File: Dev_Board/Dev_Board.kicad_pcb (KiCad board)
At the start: 2 copper layers, 48.9 x 67.6 mm, 28 parts, among them J1 Conn_01x04, J2 Conn_01x04

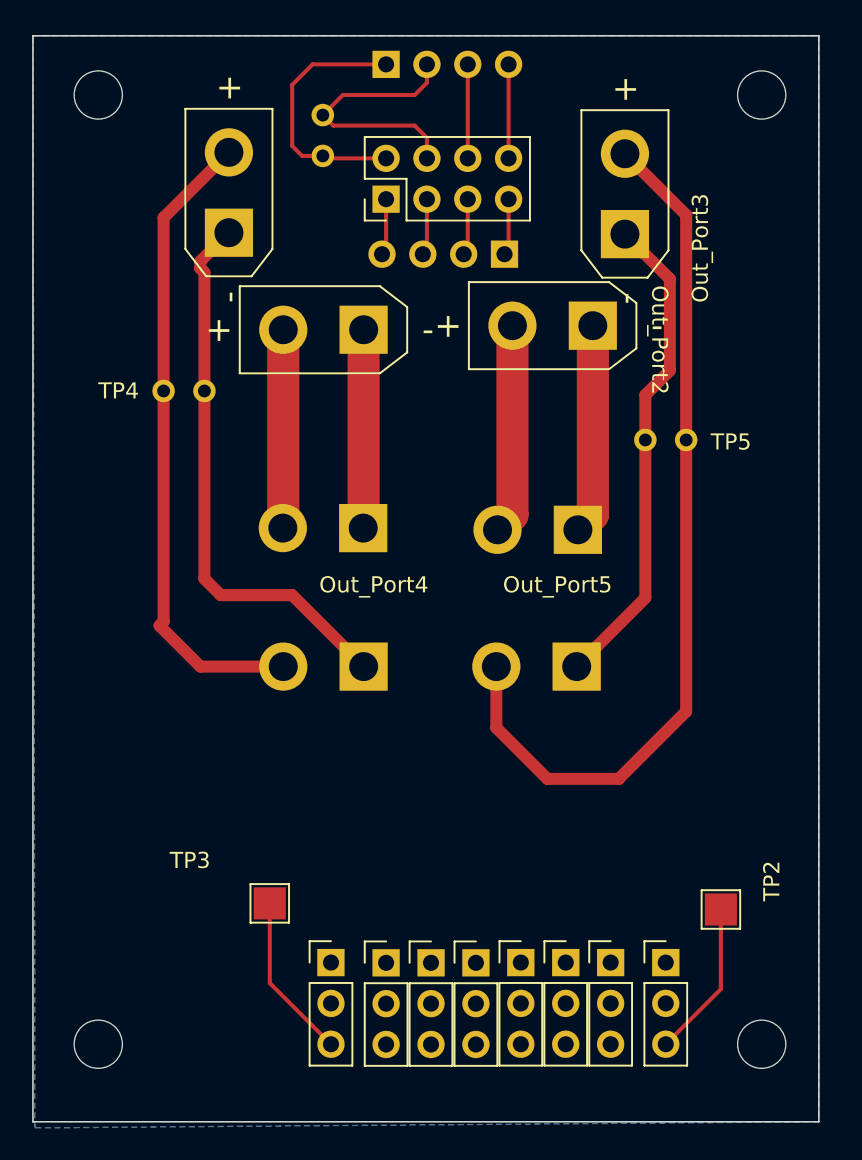
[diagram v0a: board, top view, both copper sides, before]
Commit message: added 24V plane and will resize pcb b/c dev board is 41mm
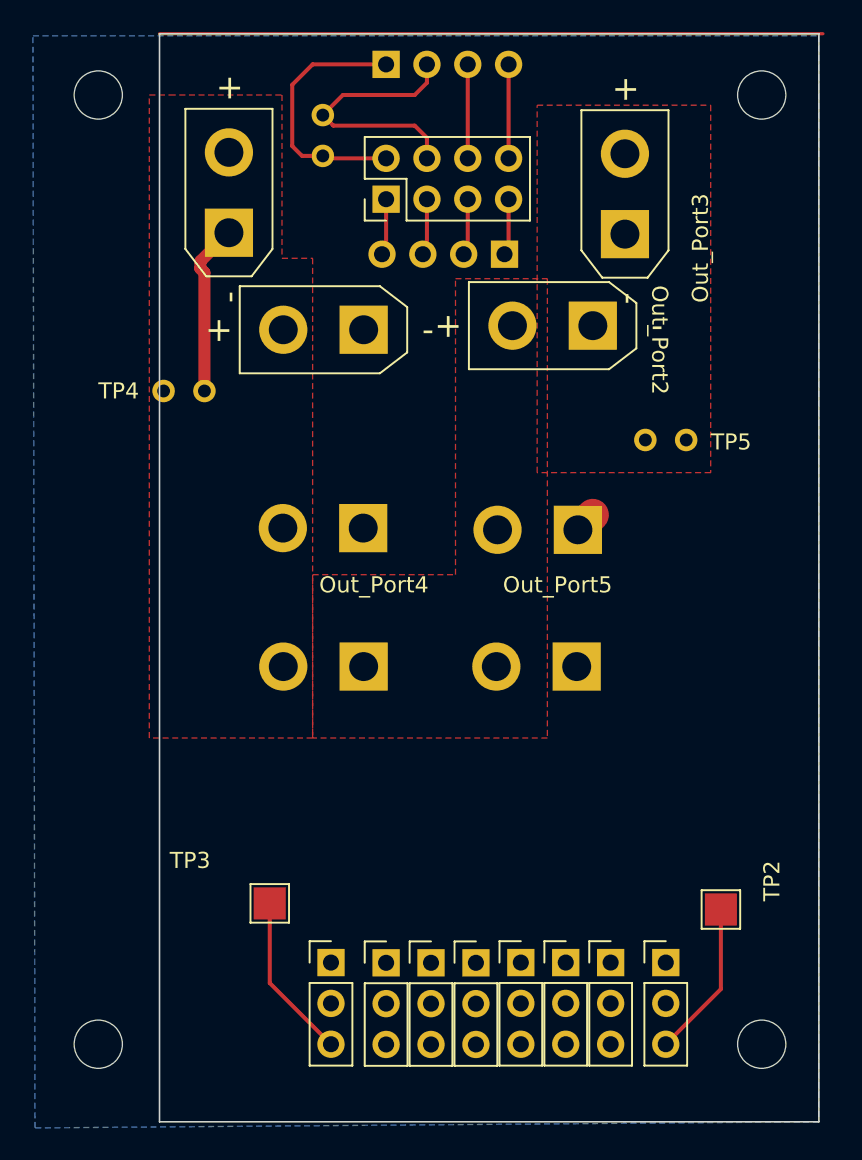
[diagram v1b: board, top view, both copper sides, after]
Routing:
- net +24V: track 120.4 -> 0.14 mm
- net GND: track 108.3 -> 29.9 mm
- added copper zone on F.Cu, net +24V
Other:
- board size 48.9 x 67.6 mm -> 41 x 67.7 mm
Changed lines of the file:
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@@
     )
   )
-  (gr_rect (start 178.181 29.972) (end 227.076 97.536)
+  (gr_line (start 186.055 29.845) (end 227.33 29.845)
+    (stroke (width 0.2) (type default)) (layer "F.Cu"))
+  (gr_rect (start 186.055 29.845) (end 227.076 97.536)
     (stroke (width 0.1) (type default)) (fill none) (layer "Edge.Cuts"))
   (segment (start 192.913 88.9) (end 196.723 92.71) (width 0.25) (layer "F.Cu") (net 1))
@@
   (segment (start 207.772 31.75) (end 207.772 37.597) (width 0.25) (layer "F.Cu") (net 27))
   (segment (start 205.232 31.75) (end 205.232 37.597) (width 0.25) (layer "F.Cu") (net 28))
-  (segment (start 218.821 41.121) (end 215.011 37.311) (width 0.75) (layer "F.Cu") (net 29))
-  (segment (start 188.595 69.215) (end 193.755 69.215) (width 0.75) (layer "F.Cu") (net 29))
-  (segment (start 218.821 55.118) (end 218.821 72.009) (width 0.75) (layer "F.Cu") (net 29))
-  (segment (start 207.01 73.025) (end 207.01 69.215) (width 0.75) (layer "F.Cu") (net 29))
-  (segment (start 208.013 48.006) (end 208.013 59.777) (width 2) (layer "F.Cu") (net 29))
   (segment (start 193.755 60.573) (end 193.728 60.6) (width 2) (layer "F.Cu") (net 29))
-  (segment (start 208.013 59.777) (end 207.084 60.706) (width 2) (layer "F.Cu") (net 29))
-  (segment (start 210.185 76.2) (end 207.01 73.025) (width 0.75) (layer "F.Cu") (net 29))
-  (segment (start 193.755 48.26) (end 193.755 60.573) (width 2) (layer "F.Cu") (net 29))
-  (segment (start 190.373 37.224) (end 186.309 41.288) (width 0.75) (layer "F.Cu") (net 29))
-  (segment (start 186.309 52.07) (end 186.309 66.421) (width 0.75) (layer "F.Cu") (net 29))
-  (segment (start 218.821 72.009) (end 214.63 76.2) (width 0.75) (layer "F.Cu") (net 29))
-  (segment (start 214.63 76.2) (end 210.185 76.2) (width 0.75) (layer "F.Cu") (net 29))
-  (segment (start 186.309 66.421) (end 186.055 66.675) (width 0.75) (layer "F.Cu") (net 29))
-  (segment (start 186.055 66.675) (end 188.595 69.215) (width 0.75) (layer "F.Cu") (net 29))
-  (segment (start 186.309 41.288) (end 186.309 52.07) (width 0.75) (layer "F.Cu") (net 29))
-  (segment (start 218.821 55.118) (end 218.821 41.121) (width 0.75) (layer "F.Cu") (net 29))
-  (segment (start 215.011 42.311) (end 217.805 45.105) (width 0.75) (layer "F.Cu") (net 30))
-  (segment (start 216.281 64.944) (end 212.01 69.215) (width 0.75) (layer "F.Cu") (net 30))
+  (segment (start 207.084 69.141) (end 207.01 69.215) (width 2) (layer "F.Cu") (net 29))
   (segment (start 194.925 37.445) (end 196.215 37.445) (width 0.25) (layer "F.Cu") (net 30))
   (segment (start 198.461 60.513) (end 198.628 60.346) (width 0.25) (layer "F.Cu") (net 30))
-  (segment (start 198.755 48.26) (end 198.755 60.573) (width 2) (layer "F.Cu") (net 30))
   (segment (start 198.561 60.767) (end 198.728 60.6) (width 0.25) (layer "F.Cu") (net 30))
   (segment (start 194.31 33.02) (end 194.31 36.83) (width 0.25) (layer "F.Cu") (net 30))
-  (segment (start 216.281 52.324) (end 216.281 55.118) (width 0.75) (layer "F.Cu") (net 30))
   (segment (start 198.655 68.674) (end 198.655 69.215) (width 0.25) (layer "F.Cu") (net 30))
   (segment (start 188.849 44.704) (end 188.849 52.07) (width 0.75) (layer "F.Cu") (net 30))
-  (segment (start 217.805 45.105) (end 217.805 50.8) (width 0.75) (layer "F.Cu") (net 30))
-  (segment (start 213.013 48.006) (end 213.013 59.777) (width 2) (layer "F.Cu") (net 30))
-  (segment (start 189.865 64.77) (end 194.31 64.77) (width 0.75) (layer "F.Cu") (net 30))
-  (segment (start 194.31 64.77) (end 198.755 69.215) (width 0.75) (layer "F.Cu") (net 30))
   (segment (start 198.755 60.573) (end 198.728 60.6) (width 2) (layer "F.Cu") (net 30))
   (segment (start 188.595 44.002) (end 188.595 44.45) (width 0.75) (layer "F.Cu") (net 30))
   (segment (start 194.31 36.83) (end 194.925 37.445) (width 0.25) (layer "F.Cu") (net 30))
   (segment (start 198.628 48.347) (end 198.969 48.006) (width 0.25) (layer "F.Cu") (net 30))
-  (segment (start 216.281 55.118) (end 216.281 64.944) (width 0.75) (layer "F.Cu") (net 30))
-  (segment (start 188.849 63.754) (end 189.865 64.77) (width 0.75) (layer "F.Cu") (net 30))
   (segment (start 188.595 44.45) (end 188.849 44.704) (width 0.75) (layer "F.Cu") (net 30))
   (segment (start 200.152 31.75) (end 195.58 31.75) (width 0.25) (layer "F.Cu") (net 30))
   (segment (start 196.367 37.597) (end 196.215 37.445) (width 0.25) (layer "F.Cu") (net 30))
-  (segment (start 188.849 52.07) (end 188.849 63.754) (width 0.75) (layer "F.Cu") (net 30))
   (segment (start 200.152 37.597) (end 196.367 37.597) (width 0.25) (layer "F.Cu") (net 30))
-  (segment (start 217.805 50.8) (end 216.281 52.324) (width 0.75) (layer "F.Cu") (net 30))
   (segment (start 213.013 59.777) (end 212.084 60.706) (width 2) (layer "F.Cu") (net 30))
   (segment (start 195.58 31.75) (end 194.31 33.02) (width 0.25) (layer "F.Cu") (net 30))
@@
   (segment (start 201.93 35.56) (end 196.87 35.56) (width 0.25) (layer "F.Cu") (net 31))
   (segment (start 202.692 32.893) (end 201.93 33.655) (width 0.25) (layer "F.Cu") (net 31))
+  (zone (net 29) (net_name "+24V") (layer "F.Cu") (hatch edge 0.5)
+    (priority 2)
+    (connect_pads (clearance 0.5))
+    (min_thickness 0.25) (filled_areas_thickness no)
+    (fill yes (thermal_gap 0.5) (thermal_bridge_width 0.5))
+    (polygon
+      (pts
+        (xy 204.47 45.085)
+        (xy 210.185 45.085)
+        (xy 210.185 73.66)
+        (xy 195.58 73.66)
+        (xy 195.58 63.5)
+        (xy 204.47 63.5)
+      )
+    )
+  )
+  (zone (net 29) (net_name "+24V") (layer "F.Cu") (hatch edge 0.5)
+    (priority 3)
+    (connect_pads (clearance 0.5))
+    (min_thickness 0.25) (filled_areas_thickness no)
+    (fill yes (thermal_gap 0.5) (thermal_bridge_width 0.5))
+    (polygon
+      (pts
+        (xy 220.345 34.29)
+        (xy 220.345 57.15)
+        (xy 209.55 57.15)
+        (xy 209.55 34.29)
+      )
+    )
+  )
+  (zone (net 29) (net_name "+24V") (layer "F.Cu") (hatch edge 0.5)
+    (priority 1)
+    (connect_pads (clearance 0.5))
+    (min_thickness 0.25) (filled_areas_thickness no)
+    (fill yes (thermal_gap 0.5) (thermal_bridge_width 0.5))
+    (polygon
+      (pts
+        (xy 193.675 33.655)
+        (xy 193.675 43.815)
+        (xy 195.58 43.815)
+        (xy 195.58 73.66)
+        (xy 185.42 73.66)
+        (xy 185.42 33.655)
+        (xy 186.69 33.655)
+      )
+    )
+  )
   (zone (net 30) (net_name "GND") (layer "B.Cu") (hatch edge 0.5)
     (connect_pads (clearance 0.5))

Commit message: fixed sizing issues and added diodes
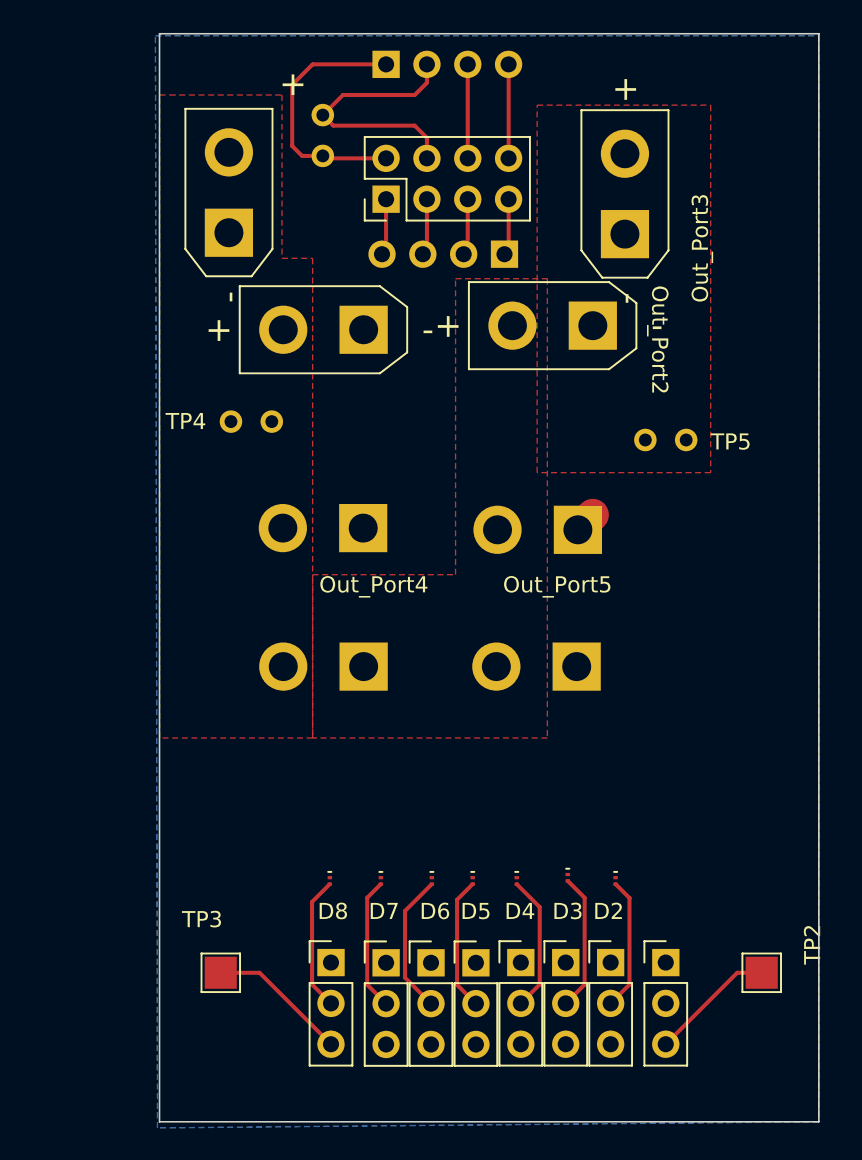
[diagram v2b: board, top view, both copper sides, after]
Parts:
- removed ? (x4): , 
- added D2: D, Diode_SMD:Nexperia_DSN0603-2_0.6x0.3mm_P0.4mm, F.Cu at (214.4, 82.5)
- added D3: D, Diode_SMD:Nexperia_DSN0603-2_0.6x0.3mm_P0.4mm, F.Cu at (211.5, 82.3)
- added D4: D, Diode_SMD:Nexperia_DSN0603-2_0.6x0.3mm_P0.4mm, F.Cu at (208.3, 82.5)
- added D5: D, Diode_SMD:Nexperia_DSN0603-2_0.6x0.3mm_P0.4mm, F.Cu at (205.5, 82.5)
- added D6: D, Diode_SMD:Nexperia_DSN0603-2_0.6x0.3mm_P0.4mm, F.Cu at (203.0, 82.5)
- added D7: D, Diode_SMD:Nexperia_DSN0603-2_0.6x0.3mm_P0.4mm, F.Cu at (199.8, 82.5)
- added D8: D, Diode_SMD:Nexperia_DSN0603-2_0.6x0.3mm_P0.4mm, F.Cu at (196.7, 82.5)
- moved TP3 5.29 mm to (189.9, 88.3)
- moved TP2 4.69 mm to (223.5, 88.3)
- moved TP4 4.60 mm to (193.0, 54.0)
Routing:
- net GND: track 29.9 -> 19.2 mm
- net /B6: track 0.00 -> 8.80 mm
- net /B3: track 0.00 -> 8.54 mm
- net /B4: track 0.00 -> 8.50 mm
- net /B8 (5V): track 0.00 -> 8.36 mm
- net /B5: track 0.00 -> 8.33 mm
- net /B7: track 0.00 -> 8.27 mm
- net /B2: track 0.00 -> 8.27 mm
- net /C1: track 9.80 -> 7.81 mm
- net /C8: track 10.3 -> 8.70 mm
